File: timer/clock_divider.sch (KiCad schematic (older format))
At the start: 2 parts, among them U1 74HC02, U2 74HC27

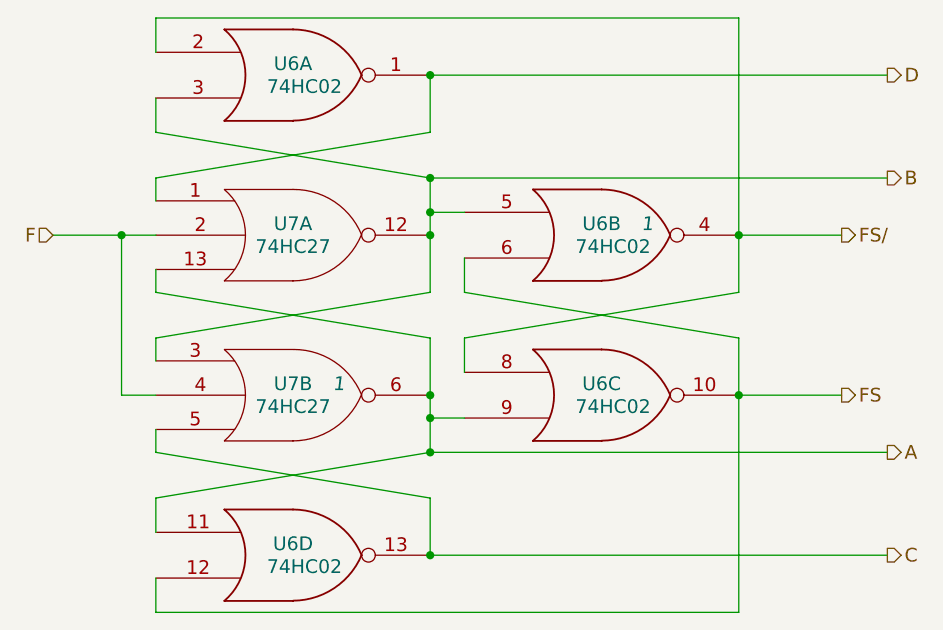
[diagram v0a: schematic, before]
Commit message: Added the start/stop logic to timer page A02-2, and introduced a new part, 74LVC07, that I think will be the solution for open drain things
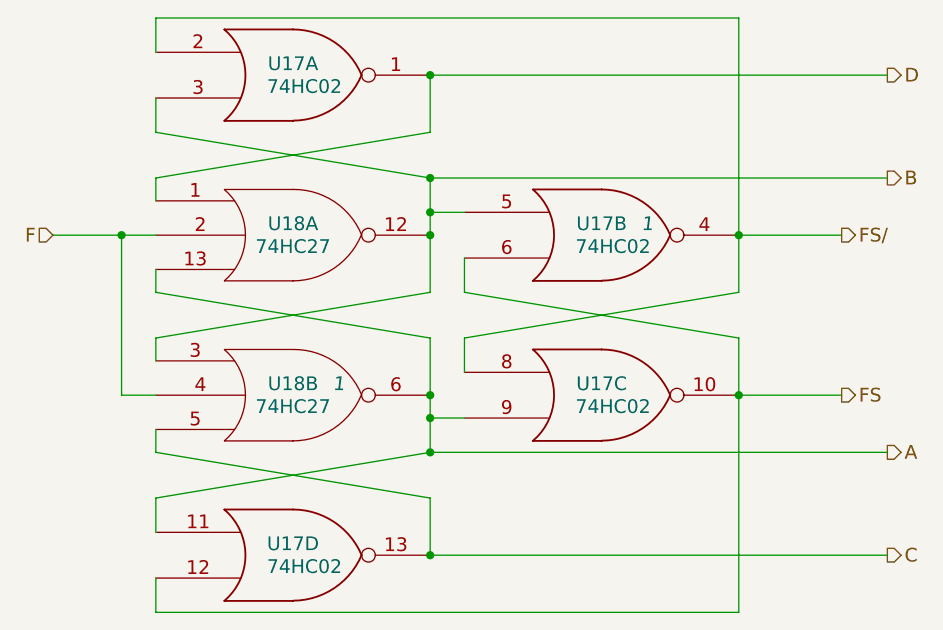
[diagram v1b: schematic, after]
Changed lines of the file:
@@
 $Descr A4 11693 8268
 encoding utf-8
-Sheet 4 6
+Sheet 6 6
 Title ""
 Date ""
@@
 AR Path="/5621C075/5627FC18/562522C4" Ref="U7"  Part="1"
 AR Path="/5626F63A/563493D5/562522C4" Ref="U18"  Part="1"
-F 0 "U7" H 2500 2850 60  0000 C CNN
+F 0 "U18" H 2500 2850 60  0000 C CNN
 F 1 "74HC27" H 2500 2750 60  0000 C CNN
 F 2 "" H 2500 2800 60  0000 C CNN
@@
 AR Path="/5621C075/5627FC18/562522CC" Ref="U7"  Part="2"
 AR Path="/5626F63A/563493D5/562522CC" Ref="U18"  Part="2"
-F 0 "U7" H 2500 3550 60  0000 C CNN
+F 0 "U18" H 2500 3550 60  0000 C CNN
 F 1 "74HC27" H 2500 3450 60  0000 C CNN
 F 2 "" H 2500 3500 60  0000 C CNN
@@
 AR Path="/5621C075/5627FC18/5625233C" Ref="U6"  Part="1"
 AR Path="/5626F63A/563493D5/5625233C" Ref="U17"  Part="1"
-F 0 "U6" H 2500 2150 60  0000 C CNN
+F 0 "U17" H 2500 2150 60  0000 C CNN
 F 1 "74HC02" H 2550 2050 60  0000 C CNN
 F 2 "" H 2500 2100 60  0000 C CNN
@@
 AR Path="/5621C075/5627FC18/56252343" Ref="U6"  Part="4"
 AR Path="/5626F63A/563493D5/56252343" Ref="U17"  Part="4"
-F 0 "U6" H 2500 4250 60  0000 C CNN
+F 0 "U17" H 2500 4250 60  0000 C CNN
 F 1 "74HC02" H 2550 4150 60  0000 C CNN
 F 2 "" H 2500 4200 60  0000 C CNN
@@
 AR Path="/5621C075/5627FC18/5625234A" Ref="U6"  Part="2"
 AR Path="/5626F63A/563493D5/5625234A" Ref="U17"  Part="2"
-F 0 "U6" H 3850 2850 60  0000 C CNN
+F 0 "U17" H 3850 2850 60  0000 C CNN
 F 1 "74HC02" H 3900 2750 60  0000 C CNN
 F 2 "" H 3850 2800 60  0000 C CNN
@@
 AR Path="/5621C075/5627FC18/56252351" Ref="U6"  Part="3"
 AR Path="/5626F63A/563493D5/56252351" Ref="U17"  Part="3"
-F 0 "U6" H 3850 3550 60  0000 C CNN
+F 0 "U17" H 3850 3550 60  0000 C CNN
 F 1 "74HC02" H 3900 3450 60  0000 C CNN
 F 2 "" H 3850 3500 60  0000 C CNN

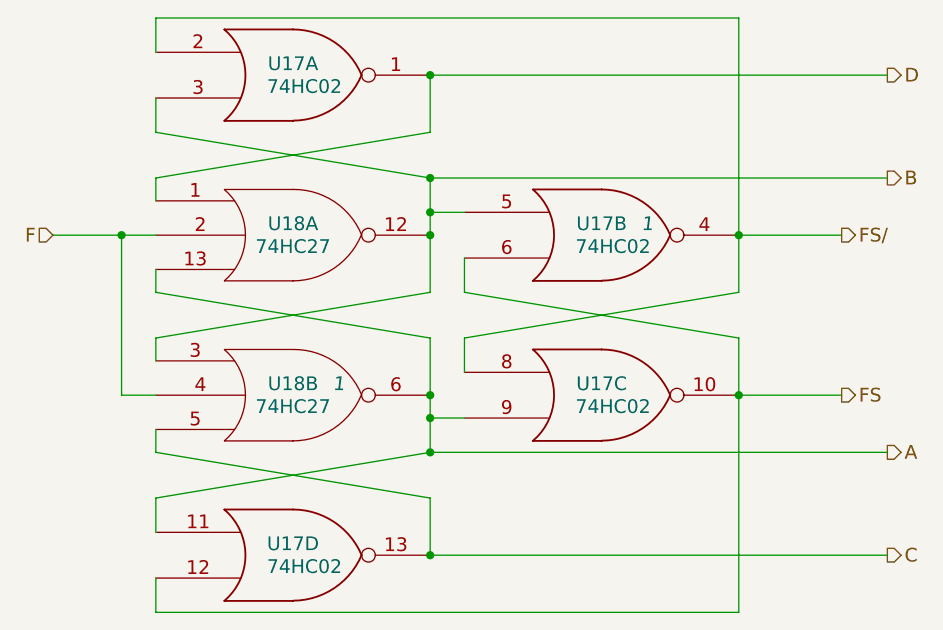
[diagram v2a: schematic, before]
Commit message: Renamed components in the timer module to fit the new numbering scheme (module_number * 1000 + part number), and updated initial conditions to make simulation happy again after fixes
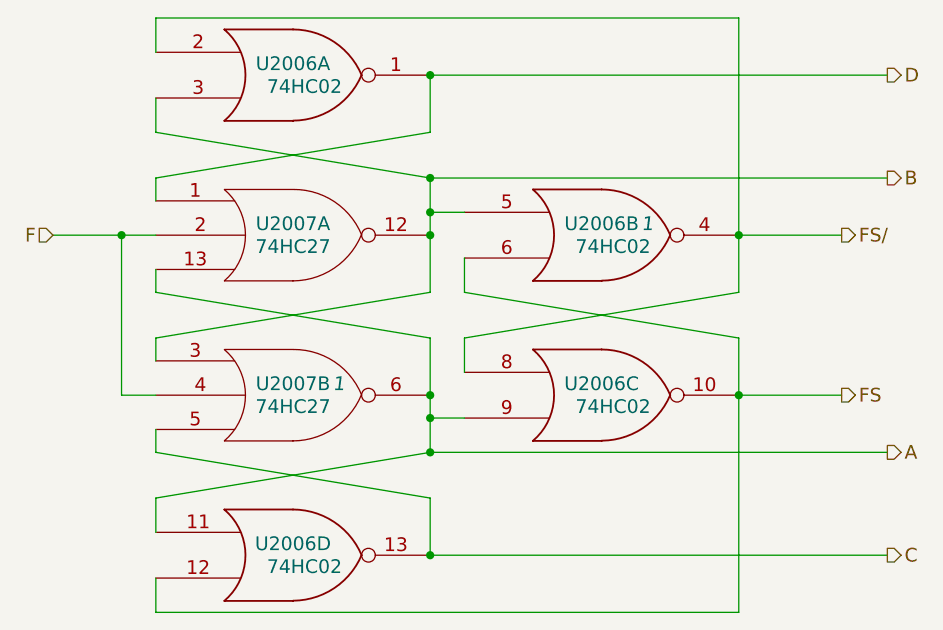
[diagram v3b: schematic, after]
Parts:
- renumbered U1 to U2001, U2 to U2002
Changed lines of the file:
@@
 $Descr A4 11693 8268
 encoding utf-8
-Sheet 6 7
+Sheet 4 7
 Title ""
 Date ""
@@
 $EndDescr
 $Comp
-L 74HC27 U2
+L 74HC27 U2002
 U 1 1 562522C4
 P 2500 2800
-AR Path="/5621C075/5625169D/562522C4" Ref="U2"  Part="1"
-AR Path="/5621C075/5627FC18/562522C4" Ref="U7"  Part="1"
-AR Path="/5626F63A/563493D5/562522C4" Ref="U18"  Part="1"
-F 0 "U18" H 2500 2850 60  0000 C CNN
+AR Path="/5621C075/5625169D/562522C4" Ref="U2002"  Part="1"
+AR Path="/5621C075/5627FC18/562522C4" Ref="U2007"  Part="1"
+AR Path="/5626F63A/563493D5/562522C4" Ref="U2018"  Part="1"
+F 0 "U2007" H 2500 2850 60  0000 C CNN
 F 1 "74HC27" H 2500 2750 60  0000 C CNN
 F 2 "" H 2500 2800 60  0000 C CNN
@@
 $EndComp
 $Comp
-L 74HC27 U2
+L 74HC27 U2002
 U 2 1 562522CC
 P 2500 3500
-AR Path="/5621C075/5625169D/562522CC" Ref="U2"  Part="2"
-AR Path="/5621C075/5627FC18/562522CC" Ref="U7"  Part="2"
-AR Path="/5626F63A/563493D5/562522CC" Ref="U18"  Part="2"
-F 0 "U18" H 2500 3550 60  0000 C CNN
+AR Path="/5621C075/5625169D/562522CC" Ref="U2002"  Part="2"
+AR Path="/5621C075/5627FC18/562522CC" Ref="U2007"  Part="2"
+AR Path="/5626F63A/563493D5/562522CC" Ref="U2018"  Part="2"
+F 0 "U2007" H 2500 3550 60  0000 C CNN
 F 1 "74HC27" H 2500 3450 60  0000 C CNN
 F 2 "" H 2500 3500 60  0000 C CNN
@@
 Connection ~ 4450 3500
 $Comp
-L 74HC02 U1
+L 74HC02 U2001
 U 1 1 5625233C
 P 2500 2100
-AR Path="/5621C075/5625169D/5625233C" Ref="U1"  Part="1"
-AR Path="/5621C075/5627FC18/5625233C" Ref="U6"  Part="1"
-AR Path="/5626F63A/563493D5/5625233C" Ref="U17"  Part="1"
-F 0 "U17" H 2500 2150 60  0000 C CNN
+AR Path="/5621C075/5625169D/5625233C" Ref="U2001"  Part="1"
+AR Path="/5621C075/5627FC18/5625233C" Ref="U2006"  Part="1"
+AR Path="/5626F63A/563493D5/5625233C" Ref="U2017"  Part="1"
+F 0 "U2006" H 2500 2150 60  0000 C CNN
 F 1 "74HC02" H 2550 2050 60  0000 C CNN
 F 2 "" H 2500 2100 60  0000 C CNN
@@
 $EndComp
 $Comp
-L 74HC02 U1
+L 74HC02 U2001
 U 4 1 56252343
 P 2500 4200
-AR Path="/5621C075/5625169D/56252343" Ref="U1"  Part="4"
-AR Path="/5621C075/5627FC18/56252343" Ref="U6"  Part="4"
-AR Path="/5626F63A/563493D5/56252343" Ref="U17"  Part="4"
-F 0 "U17" H 2500 4250 60  0000 C CNN
+AR Path="/5621C075/5625169D/56252343" Ref="U2001"  Part="4"
+AR Path="/5621C075/5627FC18/56252343" Ref="U2006"  Part="4"
+AR Path="/5626F63A/563493D5/56252343" Ref="U2017"  Part="4"
+F 0 "U2006" H 2500 4250 60  0000 C CNN
 F 1 "74HC02" H 2550 4150 60  0000 C CNN
 F 2 "" H 2500 4200 60  0000 C CNN
@@
 $EndComp
 $Comp
-L 74HC02 U1
+L 74HC02 U2001
 U 2 1 5625234A
 P 3850 2800
-AR Path="/5621C075/5625169D/5625234A" Ref="U1"  Part="2"
-AR Path="/5621C075/5627FC18/5625234A" Ref="U6"  Part="2"
-AR Path="/5626F63A/563493D5/5625234A" Ref="U17"  Part="2"
-F 0 "U17" H 3850 2850 60  0000 C CNN
+AR Path="/5621C075/5625169D/5625234A" Ref="U2001"  Part="2"
+AR Path="/5621C075/5627FC18/5625234A" Ref="U2006"  Part="2"
+AR Path="/5626F63A/563493D5/5625234A" Ref="U2017"  Part="2"
+F 0 "U2006" H 3850 2850 60  0000 C CNN
 F 1 "74HC02" H 3900 2750 60  0000 C CNN
 F 2 "" H 3850 2800 60  0000 C CNN
@@
 $EndComp
 $Comp
-L 74HC02 U1
+L 74HC02 U2001
 U 3 1 56252351
 P 3850 3500
-AR Path="/5621C075/5625169D/56252351" Ref="U1"  Part="3"
-AR Path="/5621C075/5627FC18/56252351" Ref="U6"  Part="3"
-AR Path="/5626F63A/563493D5/56252351" Ref="U17"  Part="3"
-F 0 "U17" H 3850 3550 60  0000 C CNN
+AR Path="/5621C075/5625169D/56252351" Ref="U2001"  Part="3"
+AR Path="/5621C075/5627FC18/56252351" Ref="U2006"  Part="3"
+AR Path="/5626F63A/563493D5/56252351" Ref="U2017"  Part="3"
+F 0 "U2006" H 3850 3550 60  0000 C CNN
 F 1 "74HC02" H 3900 3450 60  0000 C CNN
 F 2 "" H 3850 3500 60  0000 C CNN

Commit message: Added the strobe pulses to the timer
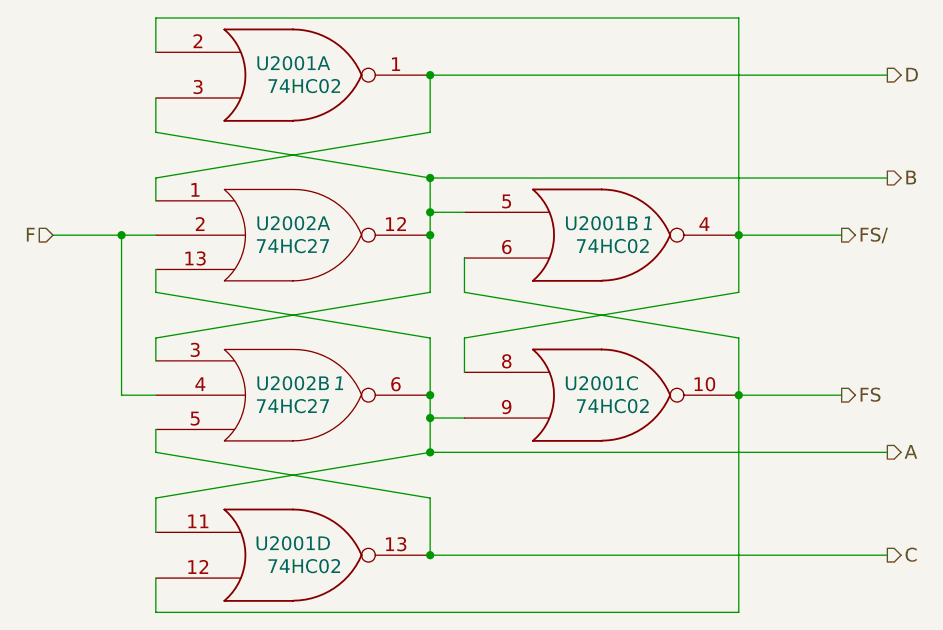
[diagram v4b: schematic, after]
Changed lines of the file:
@@
 $Descr A4 11693 8268
 encoding utf-8
-Sheet 4 7
+Sheet 3 7
 Title ""
 Date ""
@@
 AR Path="/5621C075/5627FC18/562522C4" Ref="U2007"  Part="1"
 AR Path="/5626F63A/563493D5/562522C4" Ref="U2018"  Part="1"
-F 0 "U2007" H 2500 2850 60  0000 C CNN
+F 0 "U2002" H 2500 2850 60  0000 C CNN
 F 1 "74HC27" H 2500 2750 60  0000 C CNN
 F 2 "" H 2500 2800 60  0000 C CNN
@@
 AR Path="/5621C075/5627FC18/562522CC" Ref="U2007"  Part="2"
 AR Path="/5626F63A/563493D5/562522CC" Ref="U2018"  Part="2"
-F 0 "U2007" H 2500 3550 60  0000 C CNN
+F 0 "U2002" H 2500 3550 60  0000 C CNN
 F 1 "74HC27" H 2500 3450 60  0000 C CNN
 F 2 "" H 2500 3500 60  0000 C CNN
@@
 AR Path="/5621C075/5627FC18/5625233C" Ref="U2006"  Part="1"
 AR Path="/5626F63A/563493D5/5625233C" Ref="U2017"  Part="1"
-F 0 "U2006" H 2500 2150 60  0000 C CNN
+F 0 "U2001" H 2500 2150 60  0000 C CNN
 F 1 "74HC02" H 2550 2050 60  0000 C CNN
 F 2 "" H 2500 2100 60  0000 C CNN
@@
 AR Path="/5621C075/5627FC18/56252343" Ref="U2006"  Part="4"
 AR Path="/5626F63A/563493D5/56252343" Ref="U2017"  Part="4"
-F 0 "U2006" H 2500 4250 60  0000 C CNN
+F 0 "U2001" H 2500 4250 60  0000 C CNN
 F 1 "74HC02" H 2550 4150 60  0000 C CNN
 F 2 "" H 2500 4200 60  0000 C CNN
@@
 AR Path="/5621C075/5627FC18/5625234A" Ref="U2006"  Part="2"
 AR Path="/5626F63A/563493D5/5625234A" Ref="U2017"  Part="2"
-F 0 "U2006" H 3850 2850 60  0000 C CNN
+F 0 "U2001" H 3850 2850 60  0000 C CNN
 F 1 "74HC02" H 3900 2750 60  0000 C CNN
 F 2 "" H 3850 2800 60  0000 C CNN
@@
 AR Path="/5621C075/5627FC18/56252351" Ref="U2006"  Part="3"
 AR Path="/5626F63A/563493D5/56252351" Ref="U2017"  Part="3"
-F 0 "U2006" H 3850 3550 60  0000 C CNN
+F 0 "U2001" H 3850 3550 60  0000 C CNN
 F 1 "74HC02" H 3900 3450 60  0000 C CNN
 F 2 "" H 3850 3500 60  0000 C CNN

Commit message: SUPER BROKEN: Pulled in all NOR gates into the custom library, and changed the shape of 74HC04. Some, but not all, gates have standalone power pin parts. Scaler and Timer have been updated to use the new lib and rearranged to fit the new NOTs.
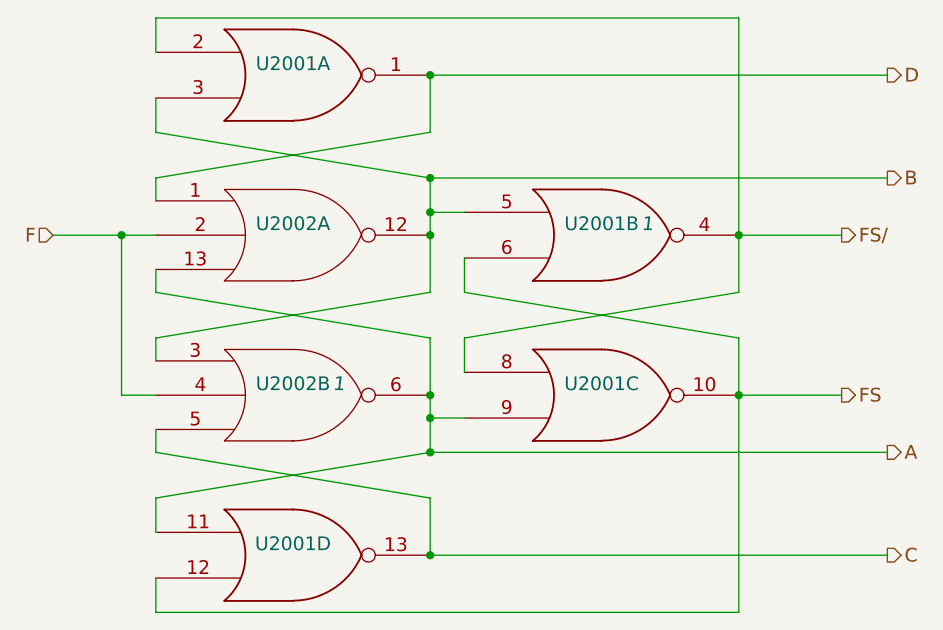
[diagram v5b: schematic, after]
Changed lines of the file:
@@
 LIBS:linear
 LIBS:regul
-LIBS:74xx
+LIBS:agc_kicad_components
 LIBS:cmos4000
 LIBS:adc-dac
@@
 LIBS:contrib
 LIBS:valves
-LIBS:agc_kicad_components
-LIBS:timer-cache
 EELAYER 25 0
 EELAYER END
@@
 AR Path="/5626F63A/563493D5/562522C4" Ref="U2018"  Part="1"
 F 0 "U2002" H 2500 2850 60  0000 C CNN
-F 1 "74HC27" H 2500 2750 60  0000 C CNN
+F 1 "74HC27" H 2500 2750 60  0001 C CNN
 F 2 "" H 2500 2800 60  0000 C CNN
 F 3 "" H 2500 2800 60  0000 C CNN
@@
 AR Path="/5626F63A/563493D5/562522CC" Ref="U2018"  Part="2"
 F 0 "U2002" H 2500 3550 60  0000 C CNN
-F 1 "74HC27" H 2500 3450 60  0000 C CNN
+F 1 "74HC27" H 2500 3450 60  0001 C CNN
 F 2 "" H 2500 3500 60  0000 C CNN
 F 3 "" H 2500 3500 60  0000 C CNN
@@
 AR Path="/5626F63A/563493D5/5625233C" Ref="U2017"  Part="1"
 F 0 "U2001" H 2500 2150 60  0000 C CNN
-F 1 "74HC02" H 2550 2050 60  0000 C CNN
+F 1 "74HC02" H 2550 2050 60  0001 C CNN
 F 2 "" H 2500 2100 60  0000 C CNN
 F 3 "" H 2500 2100 60  0000 C CNN
@@
 AR Path="/5626F63A/563493D5/56252343" Ref="U2017"  Part="4"
 F 0 "U2001" H 2500 4250 60  0000 C CNN
-F 1 "74HC02" H 2550 4150 60  0000 C CNN
+F 1 "74HC02" H 2550 4150 60  0001 C CNN
 F 2 "" H 2500 4200 60  0000 C CNN
 F 3 "" H 2500 4200 60  0000 C CNN
@@
 AR Path="/5626F63A/563493D5/5625234A" Ref="U2017"  Part="2"
 F 0 "U2001" H 3850 2850 60  0000 C CNN
-F 1 "74HC02" H 3900 2750 60  0000 C CNN
+F 1 "74HC02" H 3900 2750 60  0001 C CNN
 F 2 "" H 3850 2800 60  0000 C CNN
 F 3 "" H 3850 2800 60  0000 C CNN
@@
 AR Path="/5626F63A/563493D5/56252351" Ref="U2017"  Part="3"
 F 0 "U2001" H 3850 3550 60  0000 C CNN
-F 1 "74HC02" H 3900 3450 60  0000 C CNN
+F 1 "74HC02" H 3900 3450 60  0001 C CNN
 F 2 "" H 3850 3500 60  0000 C CNN
 F 3 "" H 3850 3500 60  0000 C CNN

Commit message: Added switched and unswitched power nets to the Timer. Also fixed a few glitches in the new library parts.
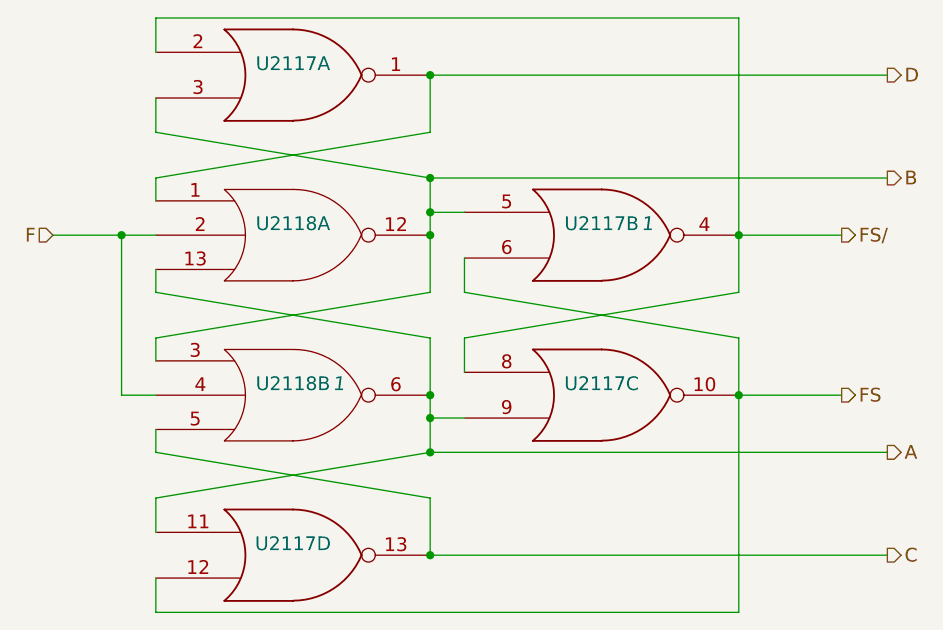
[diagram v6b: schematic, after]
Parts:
- renumbered U2001 to U2101, U2002 to U2102
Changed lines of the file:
@@
 LIBS:contrib
 LIBS:valves
+LIBS:timer-cache
 EELAYER 25 0
 EELAYER END
 $Descr A4 11693 8268
 encoding utf-8
-Sheet 3 7
+Sheet 6 7
 Title ""
 Date ""
@@
 $EndDescr
 $Comp
-L 74HC27 U2002
+L 74HC27 U2102
 U 1 1 562522C4
 P 2500 2800
-AR Path="/5621C075/5625169D/562522C4" Ref="U2002"  Part="1"
-AR Path="/5621C075/5627FC18/562522C4" Ref="U2007"  Part="1"
-AR Path="/5626F63A/563493D5/562522C4" Ref="U2018"  Part="1"
-F 0 "U2002" H 2500 2850 60  0000 C CNN
+AR Path="/5621C075/5625169D/562522C4" Ref="U2102"  Part="1"
+AR Path="/5621C075/5627FC18/562522C4" Ref="U2107"  Part="1"
+AR Path="/5626F63A/563493D5/562522C4" Ref="U2118"  Part="1"
+F 0 "U2118" H 2500 2850 60  0000 C CNN
 F 1 "74HC27" H 2500 2750 60  0001 C CNN
 F 2 "" H 2500 2800 60  0000 C CNN
@@
 $EndComp
 $Comp
-L 74HC27 U2002
+L 74HC27 U2102
 U 2 1 562522CC
 P 2500 3500
-AR Path="/5621C075/5625169D/562522CC" Ref="U2002"  Part="2"
-AR Path="/5621C075/5627FC18/562522CC" Ref="U2007"  Part="2"
-AR Path="/5626F63A/563493D5/562522CC" Ref="U2018"  Part="2"
-F 0 "U2002" H 2500 3550 60  0000 C CNN
+AR Path="/5621C075/5625169D/562522CC" Ref="U2102"  Part="2"
+AR Path="/5621C075/5627FC18/562522CC" Ref="U2107"  Part="2"
+AR Path="/5626F63A/563493D5/562522CC" Ref="U2118"  Part="2"
+F 0 "U2118" H 2500 3550 60  0000 C CNN
 F 1 "74HC27" H 2500 3450 60  0001 C CNN
 F 2 "" H 2500 3500 60  0000 C CNN
@@
 Connection ~ 4450 3500
 $Comp
-L 74HC02 U2001
+L 74HC02 U2101
 U 1 1 5625233C
 P 2500 2100
-AR Path="/5621C075/5625169D/5625233C" Ref="U2001"  Part="1"
-AR Path="/5621C075/5627FC18/5625233C" Ref="U2006"  Part="1"
-AR Path="/5626F63A/563493D5/5625233C" Ref="U2017"  Part="1"
-F 0 "U2001" H 2500 2150 60  0000 C CNN
+AR Path="/5621C075/5625169D/5625233C" Ref="U2101"  Part="1"
+AR Path="/5621C075/5627FC18/5625233C" Ref="U2106"  Part="1"
+AR Path="/5626F63A/563493D5/5625233C" Ref="U2117"  Part="1"
+F 0 "U2117" H 2500 2150 60  0000 C CNN
 F 1 "74HC02" H 2550 2050 60  0001 C CNN
 F 2 "" H 2500 2100 60  0000 C CNN
@@
 $EndComp
 $Comp
-L 74HC02 U2001
+L 74HC02 U2101
 U 4 1 56252343
 P 2500 4200
-AR Path="/5621C075/5625169D/56252343" Ref="U2001"  Part="4"
-AR Path="/5621C075/5627FC18/56252343" Ref="U2006"  Part="4"
-AR Path="/5626F63A/563493D5/56252343" Ref="U2017"  Part="4"
-F 0 "U2001" H 2500 4250 60  0000 C CNN
+AR Path="/5621C075/5625169D/56252343" Ref="U2101"  Part="4"
+AR Path="/5621C075/5627FC18/56252343" Ref="U2106"  Part="4"
+AR Path="/5626F63A/563493D5/56252343" Ref="U2117"  Part="4"
+F 0 "U2117" H 2500 4250 60  0000 C CNN
 F 1 "74HC02" H 2550 4150 60  0001 C CNN
 F 2 "" H 2500 4200 60  0000 C CNN
@@
 $EndComp
 $Comp
-L 74HC02 U2001
+L 74HC02 U2101
 U 2 1 5625234A
 P 3850 2800
-AR Path="/5621C075/5625169D/5625234A" Ref="U2001"  Part="2"
-AR Path="/5621C075/5627FC18/5625234A" Ref="U2006"  Part="2"
-AR Path="/5626F63A/563493D5/5625234A" Ref="U2017"  Part="2"
-F 0 "U2001" H 3850 2850 60  0000 C CNN
+AR Path="/5621C075/5625169D/5625234A" Ref="U2101"  Part="2"
+AR Path="/5621C075/5627FC18/5625234A" Ref="U2106"  Part="2"
+AR Path="/5626F63A/563493D5/5625234A" Ref="U2117"  Part="2"
+F 0 "U2117" H 3850 2850 60  0000 C CNN
 F 1 "74HC02" H 3900 2750 60  0001 C CNN
 F 2 "" H 3850 2800 60  0000 C CNN
@@
 $EndComp
 $Comp
-L 74HC02 U2001
+L 74HC02 U2101
 U 3 1 56252351
 P 3850 3500
-AR Path="/5621C075/5625169D/56252351" Ref="U2001"  Part="3"
-AR Path="/5621C075/5627FC18/56252351" Ref="U2006"  Part="3"
-AR Path="/5626F63A/563493D5/56252351" Ref="U2017"  Part="3"
-F 0 "U2001" H 3850 3550 60  0000 C CNN
+AR Path="/5621C075/5625169D/56252351" Ref="U2101"  Part="3"
+AR Path="/5621C075/5627FC18/56252351" Ref="U2106"  Part="3"
+AR Path="/5626F63A/563493D5/56252351" Ref="U2117"  Part="3"
+F 0 "U2117" H 3850 3550 60  0000 C CNN
 F 1 "74HC02" H 3900 3450 60  0001 C CNN
 F 2 "" H 3850 3500 60  0000 C CNN
